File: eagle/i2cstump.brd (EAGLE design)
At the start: 31.2 x 19 mm, 22 parts, among them IC1 ATTINY85, IC2 REG1117, J1 I2C-5V, J2 I2C-3V3, J3 AVR_SPI_PROG_3X2TESTPOINTS, Q1 220mA/50V/3.5Ω, Q2 220mA/50V/3.5Ω, X1 USBPCB

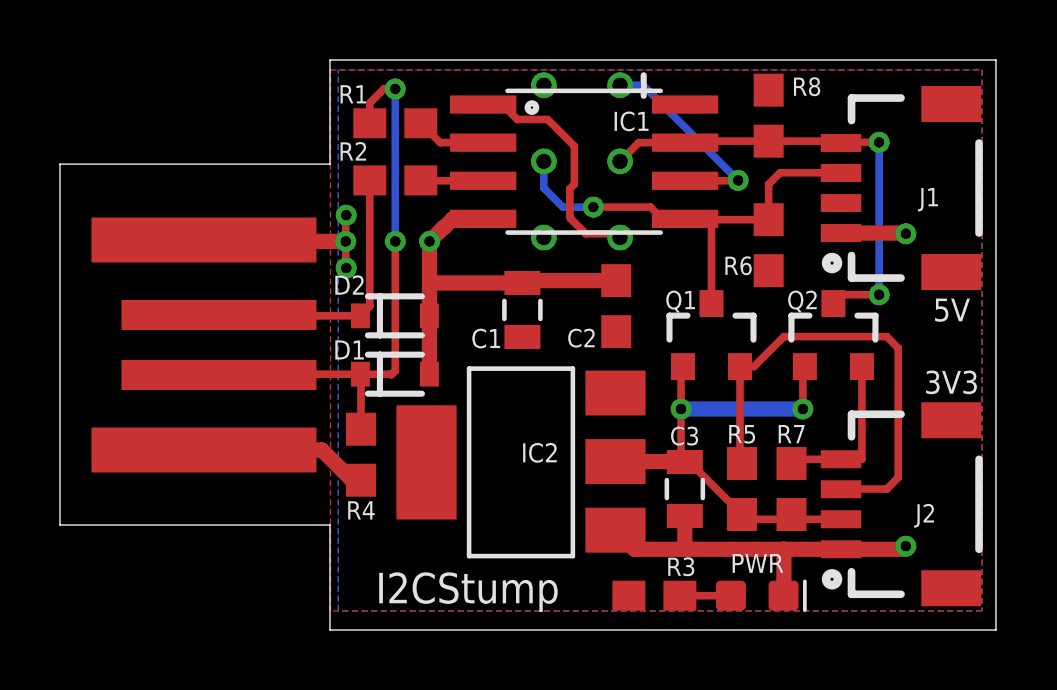
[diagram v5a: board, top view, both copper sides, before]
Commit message: Version 3.0 -- with 3mm screwhole in the center. Aligned J1/J2 to be 0.76mm from the edges. Replaced bulky AM1117 (SOT223) with a MCP1700 (SOT23)
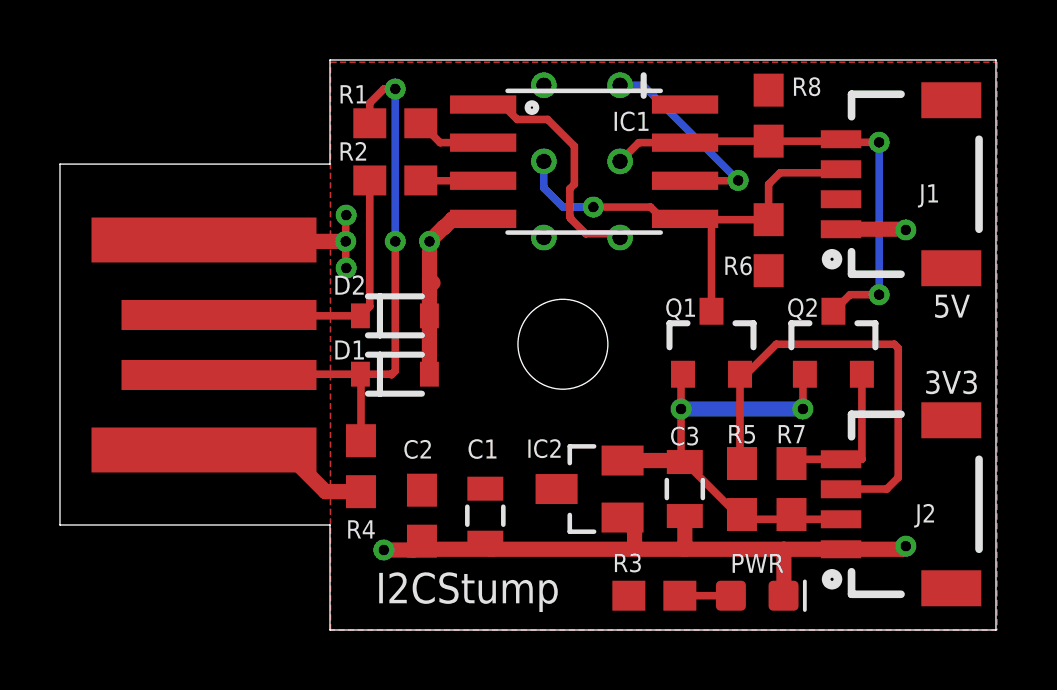
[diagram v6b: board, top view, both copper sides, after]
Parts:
- IC2: value REG1117 -> MCP1703CB; device burr-brown:SOT223 -> linear:SOT23
- moved C2 9.53 mm to (12.1, 3.81), turned to 270 degrees
- moved C1 6.97 mm to (14.2, 3.81), turned to 270 degrees
- moved IC2 2.45 mm to (17.7, 4.70)
- moved R4 0.38 mm to (10.0, 5.46)
- moved Q1 0.25 mm to (21.7, 9.53)
- moved Q2 0.25 mm to (25.8, 9.53)
- moved J1 0.13 mm to (26.0, 14.9)
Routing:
- net GND: track 34.2 -> 37.3 mm, vias 6 -> 7
- net +3V3: track 17.2 -> 16.4 mm
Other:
- board text added: "github.com/pimvanpelt/i2cstump I2C, 3.3V & 5V Version 3.0"
- board text removed: "github.com/pimvanpelt/i2cstump I2C, 3.3V & 5V Version 2.0"

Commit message: Change R3 to 390R, 2.2V green LED, not too bright
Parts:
- R3: value 1k5 -> 390R
- R4: value 1k5 -> 2k2
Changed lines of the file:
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@@
 <drawing>
 <settings>
-<setting alwaysvectorfont="yes"/>
+<setting alwaysvectorfont="no"/>
 <setting keepoldvectorfont="yes"/>
 <setting verticaltext="up"/>
@@
 <attribute name="VALUE" x="24.384" y="17.145" size="0.6096" layer="27" font="vector" ratio="20" rot="R90" align="top-center"/>
 </element>
-<element name="R4" library="SparkFun-Resistors" library_urn="urn:adsk.eagle:library:532" package="0603" package3d_urn="urn:adsk.eagle:package:39650/1" value="1k5" x="10.033" y="5.461" smashed="yes" rot="R270">
+<element name="R4" library="SparkFun-Resistors" library_urn="urn:adsk.eagle:library:532" package="0603" package3d_urn="urn:adsk.eagle:package:39650/1" value="2k2" x="10.033" y="5.461" smashed="yes" rot="R270">
 <attribute name="NAME" x="10.033" y="3.048" size="0.6096" layer="25" font="vector" ratio="20" align="bottom-center"/>
 <attribute name="PROD_ID" value=" " x="10.033" y="5.207" size="1.778" layer="27" rot="R270" display="off"/>
@@
 <attribute name="VALUE" x="23.241" y="0.508" size="0.6096" layer="27" font="vector" ratio="20" align="top-center"/>
 </element>
-<element name="R3" library="SparkFun-Resistors" library_urn="urn:adsk.eagle:library:532" package="0603" package3d_urn="urn:adsk.eagle:package:39650/1" value="1k5" x="19.812" y="1.143" smashed="yes" rot="R180">
+<element name="R3" library="SparkFun-Resistors" library_urn="urn:adsk.eagle:library:532" package="0603" package3d_urn="urn:adsk.eagle:package:39650/1" value="390R" x="19.812" y="1.143" smashed="yes" rot="R180">
 <attribute name="NAME" x="18.923" y="2.54" size="0.6096" layer="25" font="vector" ratio="20" rot="R180" align="bottom-center"/>
 <attribute name="PROD_ID" value=" " x="19.812" y="1.143" size="1.778" layer="27" rot="R180" display="off"/>
